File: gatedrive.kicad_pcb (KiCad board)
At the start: 2 copper layers, 50.8 x 54.4 mm, 26 parts, among them IC1 HCPL-316J, IC2 IXDD614PI, p1 POWER SUPPLY CONNECTOR., p2 IGBT CONNECTOR., p3 CONTROLLER CONNECTOR.

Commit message: Prototype
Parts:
- added C4: 0.1uF, Capacitors_ThroughHole:C_Disc_D3_P2.5, F.Cu at (125.7, 122.7)
- added C5: 0.1uF, Capacitors_ThroughHole:C_Disc_D3_P2.5, F.Cu at (140.8, 113.5)
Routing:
- net Net-(D2-Pad2): track 38.5 -> 30.4 mm
- net G: track 94.1 -> 89.0 mm
- net 15V: track 51.4 -> 54.2 mm
- net -5V: track 69.5 -> 72.3 mm
- net Net-(D2-Pad1): track 23.7 -> 21.9 mm
- net Net-(IC1-Pad11): track 54.3 -> 53.2 mm

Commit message: sending to m.n
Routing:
- net MICSUPP: track 23.4 -> 22.8 mm
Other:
- board text removed: "5v"
- board text removed: "T1"
- board text removed: "fault"
- board text removed: "gnd1"
- board text removed: "reset"
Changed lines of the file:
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@@
     (area 106.419714 66.608 183.648286 128.938001)
     (thickness 1.6)
-    (drawings 24)
+    (drawings 19)
     (tracks 135)
     (zones 0)
@@
   )
   (setup
-    (last_trace_width 1.016)
+    (last_trace_width 0.254)
     (user_trace_width 0.254)
     (user_trace_width 0.6)
@@
     (add_net ~RST)
   )
+  (module Socket_Strips:Socket_Strip_Straight_1x05 (layer F.Cu)
+    (at 124.333 79.4385 270)
+    (descr "Through hole socket strip")
+    (tags "socket strip")
+    (fp_text reference p3 (at -3.7846 -4.4196 270) (layer F.SilkS)
+      (effects (font (size 1 1) (thickness 0.15)))
+    )
+    (fp_text value "CONTROLLER CONNECTOR." (at 4.572 -4.064 270) (layer F.Fab)
+      (effects (font (size 1 1) (thickness 0.15)))
+    )
+    (fp_line (start 3.9116 3.2004) (end 3.9116 4.2164) (layer F.SilkS) (width 0.1))
+    (fp_line (start 6.3881 3.2004) (end 6.3881 4.2164) (layer F.SilkS) (width 0.1))
+    (fp_line (start 8.9916 3.2004) (end 8.9916 4.2164) (layer F.SilkS) (width 0.1))
+    (fp_line (start 11.5316 4.2164) (end 11.5316 3.2004) (layer F.SilkS) (width 0.1))
+    (fp_line (start -1.4224 4.2672) (end 11.5316 4.2672) (layer F.SilkS) (width 0.1))
+    (fp_line (start -1.4224 3.2004) (end -1.4224 4.2164) (layer F.SilkS) (width 0.1))
+    (fp_line (start 1.6256 3.2004) (end 1.6256 4.2164) (layer F.SilkS) (width 0.1))
+    (fp_text user ~FAULT (at 0.1143 3.683 270) (layer F.SilkS)
+      (effects (font (size 0.6 0.6) (thickness 0.1)))
+    )
+    (fp_text user T1 (at 10.2743 3.683 270) (layer F.SilkS)
+      (effects (font (size 0.6 0.6) (thickness 0.1)))
+    )
+    (fp_text user ~RST (at 2.6543 3.683 270) (layer F.SilkS)
+      (effects (font (size 0.6 0.6) (thickness 0.1)))
+    )
+    (fp_text user 5V (at 5.1943 3.683 270) (layer F.SilkS)
+      (effects (font (size 0.6 0.6) (thickness 0.1)))
+    )
+    (fp_text user GND1 (at 7.7343 3.683 270) (layer F.SilkS)
+      (effects (font (size 0.6 0.6) (thickness 0.1)))
+    )
+    (fp_line (start -1.8796 3.175) (end -1.8796 -3.429) (layer F.SilkS) (width 0.1))
+    (fp_line (start 12.0142 3.2004) (end -1.8796 3.2004) (layer F.SilkS) (width 0.1))
+    (fp_line (start 12.0142 -3.429) (end 12.0142 3.175) (layer F.SilkS) (width 0.1))
+    (fp_line (start 12.0142 -3.429) (end -1.8796 -3.429) (layer F.SilkS) (width 0.1))
+    (fp_line (start -1.8796 -3.429) (end -1.8796 3.2004) (layer F.CrtYd) (width 0.05))
+    (fp_line (start 12.0142 -3.429) (end 12.0142 3.175) (layer F.CrtYd) (width 0.05))
+    (fp_line (start -1.8796 -3.429) (end 12.0142 -3.429) (layer F.CrtYd) (width 0.05))
+    (fp_line (start -1.8796 3.2004) (end 12.0142 3.2004) (layer F.CrtYd) (width 0.05))
+    (pad 1 thru_hole oval (at 0.0889 0.0254 270) (size 1.7272 2.032) (drill 0.5) (layers *.Cu *.Mask F.SilkS)
+      (net 5 ~FAULT))
+    (pad 2 thru_hole oval (at 2.6289 0.0254 270) (size 1.7272 2.032) (drill 0.5) (layers *.Cu *.Mask F.SilkS)
+      (net 9 ~RST))
+    (pad 3 thru_hole oval (at 5.1689 0.0254 270) (size 1.7272 2.032) (drill 0.5) (layers *.Cu *.Mask F.SilkS)
+      (net 4 MICSUPP))
+    (pad 4 thru_hole oval (at 7.7089 0.0254 270) (size 1.7272 2.032) (drill 0.5) (layers *.Cu *.Mask F.SilkS)
+      (net 7 GND1))
+    (pad 5 thru_hole oval (at 10.2489 0.0254 270) (size 1.7272 2.032) (drill 0.5) (layers *.Cu *.Mask F.SilkS)
+      (net 10 T1))
+    (model Socket_Strips.3dshapes/Socket_Strip_Straight_1x05.wrl
+      (at (xyz 0.2 0 0))
+      (scale (xyz 1 1 1))
+      (rotate (xyz 0 0 180))
+    )
+  )
   (module Capacitors_ThroughHole:C_Disc_D3_P2.5 (layer F.Cu)
     (at 125.73 122.682)
@@
     (descr "Resistor, Axial,  RM 10mm, 1/3W,")
     (tags "Resistor, Axial, RM 10mm, 1/3W,")
-    (fp_text reference R2 (at 0 -2.159) (layer F.SilkS)
+    (fp_text reference R2 (at 0 0) (layer F.SilkS)
       (effects (font (size 1 1) (thickness 0.15)))
     )
@@
       (scale (xyz 0.4 0.4 0.4))
       (rotate (xyz 0 0 0))
-    )
-  )
-  (module Socket_Strips:Socket_Strip_Straight_1x05 (layer F.Cu)
-    (at 124.333 79.4385 270)
-    (descr "Through hole socket strip")
-    (tags "socket strip")
-    (fp_text reference p3 (at -2.3114 0.4445 540) (layer F.SilkS)
-      (effects (font (size 1 1) (thickness 0.15)))
-    )
-    (fp_text value "CONTROLLER CONNECTOR." (at 4.572 -3.556 270) (layer F.Fab)
-      (effects (font (size 1 1) (thickness 0.15)))
-    )
-    (fp_line (start -3.175 -2.54) (end -3.175 3.175) (layer F.CrtYd) (width 0.05))
-    (fp_line (start 13.335 -2.54) (end 13.335 3.2385) (layer F.CrtYd) (width 0.05))
-    (fp_line (start -3.175 -2.54) (end 13.335 -2.54) (layer F.CrtYd) (width 0.05))
-    (fp_line (start -3.175 3.175) (end 13.335 3.2385) (layer F.CrtYd) (width 0.05))
-    (fp_line (start 1.5875 1.651) (end 11.7475 1.651) (layer F.SilkS) (width 0.15))
-    (fp_line (start 11.7475 1.651) (end 11.7475 -0.889) (layer F.SilkS) (width 0.15))
-    (fp_line (start 11.7475 -0.889) (end 1.5875 -0.889) (layer F.SilkS) (width 0.15))
-    (fp_line (start -1.2325 1.931) (end 0.3175 1.931) (layer F.SilkS) (width 0.15))
-    (fp_line (start 1.5875 1.651) (end 1.5875 -0.889) (layer F.SilkS) (width 0.15))
-    (fp_line (start 0.3175 -1.169) (end -1.2325 -1.169) (layer F.SilkS) (width 0.15))
-    (fp_line (start -1.2325 -1.169) (end -1.2325 1.931) (layer F.SilkS) (width 0.15))
-    (pad 1 thru_hole oval (at 0.3175 0.381 270) (size 1.7272 2.032) (drill 0.5) (layers *.Cu *.Mask F.SilkS)
-      (net 5 ~FAULT))
-    (pad 2 thru_hole oval (at 2.8575 0.381 270) (size 1.7272 2.032) (drill 0.5) (layers *.Cu *.Mask F.SilkS)
-      (net 9 ~RST))
-    (pad 3 thru_hole oval (at 5.3975 0.381 270) (size 1.7272 2.032) (drill 0.5) (layers *.Cu *.Mask F.SilkS)
-      (net 4 MICSUPP))
-    (pad 4 thru_hole oval (at 7.9375 0.381 270) (size 1.7272 2.032) (drill 0.5) (layers *.Cu *.Mask F.SilkS)
-      (net 7 GND1))
-    (pad 5 thru_hole oval (at 10.4775 0.381 270) (size 1.7272 2.032) (drill 0.5) (layers *.Cu *.Mask F.SilkS)
-      (net 10 T1))
-    (model Socket_Strips.3dshapes/Socket_Strip_Straight_1x05.wrl
-      (at (xyz 0.2 0 0))
-      (scale (xyz 1 1 1))
-      (rotate (xyz 0 0 180))
     )
   )
@@
     (descr "Capacitor 3mm Disc, Pitch 2.5mm")
     (tags Capacitor)
-    (fp_text reference C1 (at 1.143 -2.286 90) (layer F.SilkS)
+    (fp_text reference C1 (at 1.2046 0.0127 360) (layer F.SilkS)
       (effects (font (size 1 1) (thickness 0.15)))
     )
@@
     (arrow2a (pts (xy 172.466 70.866) (xy 171.879579 71.992504)))
     (arrow2b (pts (xy 172.466 70.866) (xy 173.052421 71.992504)))
-  )
-  (gr_text T1 (at 121.158 89.916) (layer F.SilkS)
-    (effects (font (size 0.7 0.7) (thickness 0.1)))
-  )
-  (gr_text gnd1 (at 121.158 87.376) (layer F.SilkS)
-    (effects (font (size 0.7 0.7) (thickness 0.1)))
-  )
-  (gr_text 5v (at 120.904 84.836) (layer F.SilkS)
-    (effects (font (size 0.7 0.7) (thickness 0.1)))
-  )
-  (gr_text "reset\n" (at 120.904 82.423) (layer F.SilkS)
-    (effects (font (size 0.7 0.7) (thickness 0.1)))
-  )
-  (gr_text "fault\n" (at 120.904 79.756) (layer F.SilkS)
-    (effects (font (size 0.7 0.7) (thickness 0.1)))
   )
   (gr_text G (at 166.497 109.982) (layer F.SilkS)
@@
   (segment (start 141.175 76.835) (end 141.175 76.024) (width 0.635) (layer B.Cu) (net 3) (status 10))
   (segment (start 141.175 76.024) (end 139.446 74.295) (width 0.635) (layer B.Cu) (net 3) (status 20))
-  (segment (start 122.34164 73.533) (end 123.117999 74.309359) (width 1.27) (layer B.Cu) (net 4) (status 10))
-  (segment (start 123.117999 74.309359) (end 123.117999 76.780001) (width 1.27) (layer B.Cu) (net 4))
+  (segment (start 122.722067 84.836) (end 123.952 84.836) (width 1.27) (layer B.Cu) (net 4))
   (segment (start 121.881127 83.99506) (end 122.722067 84.836) (width 1.27) (layer B.Cu) (net 4))
-  (segment (start 123.117999 76.780001) (end 121.881127 78.016873) (width 1.27) (layer B.Cu) (net 4))
   (segment (start 121.881127 78.016873) (end 121.881127 83.99506) (width 1.27) (layer B.Cu) (net 4))
-  (segment (start 122.722067 84.836) (end 123.952 84.836) (width 1.27) (layer B.Cu) (net 4) (status 20))
+  (segment (start 122.350617 77.547383) (end 121.881127 78.016873) (width 1.27) (layer B.Cu) (net 4))
+  (segment (start 122.350617 73.541977) (end 122.350617 77.547383) (width 1.27) (layer B.Cu) (net 4))
+  (segment (start 122.34164 73.533) (end 122.350617 73.541977) (width 1.27) (layer B.Cu) (net 4))
   (segment (start 129.2225 81.875) (end 130.5325 83.185) (width 0.6) (layer B.Cu) (net 4) (status 10))
   (segment (start 130.5325 83.185) (end 131.875 83.185) (width 0.6) (layer B.Cu) (net 4) (status 20))

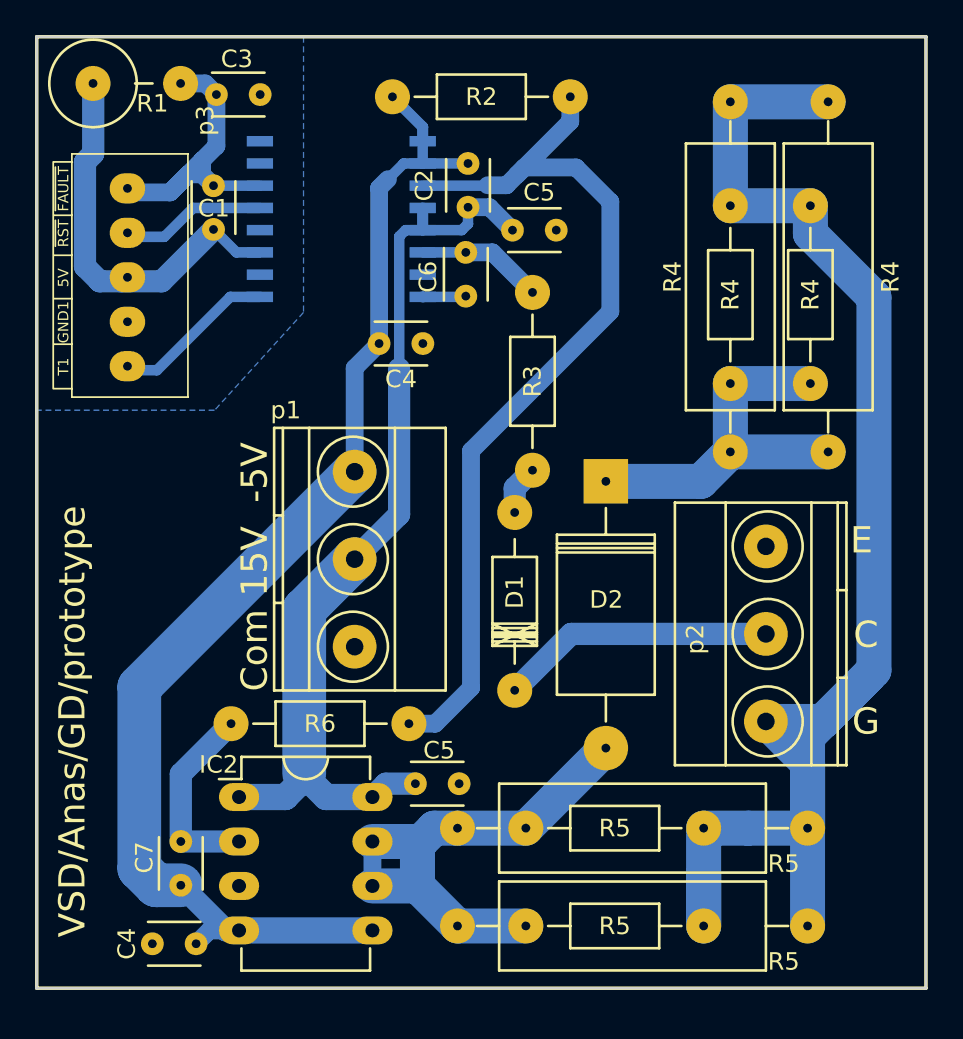
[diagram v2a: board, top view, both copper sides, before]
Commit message: updsting hcpl-316j ic footprint and layout
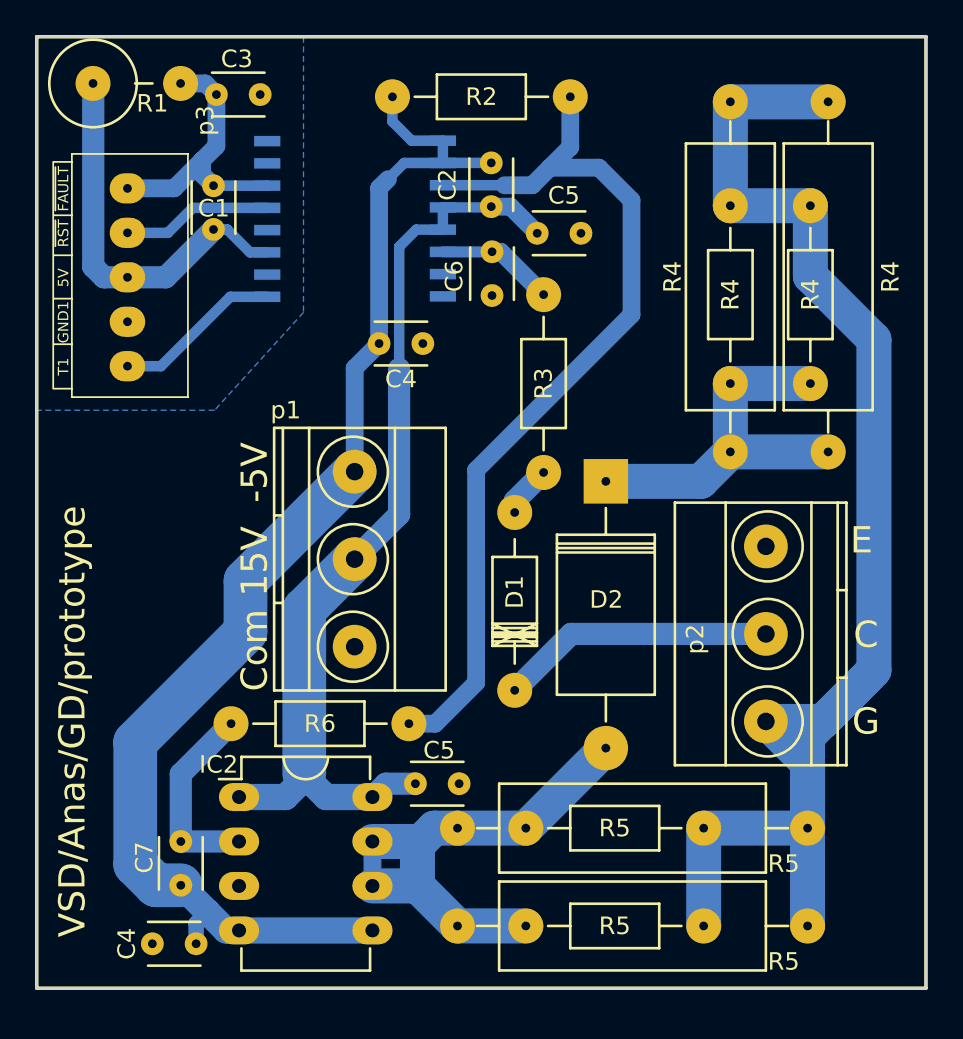
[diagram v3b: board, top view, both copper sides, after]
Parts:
- moved C6 1.50 mm to (145.1, 83.1)
- moved C5 1.42 mm to (147.7, 82.1)
- moved C2 1.33 mm to (145.1, 80.6)
- moved IC1 1.15 mm to (137.7, 81.3)
- moved R3 0.65 mm to (148.1, 90.7)
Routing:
- net G: track 89.0 -> 85.9 mm
- net COM: track 2.49 -> 0.07 mm
- net -5V: track 72.3 -> 74.6 mm
- net ~FAULT: track 18.4 -> 16.1 mm
- net Net-(IC1-Pad11): track 53.2 -> 52.6 mm

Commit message: cleaning the repo
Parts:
- removed C4 (x2): 0.1uF, Capacitors_ThroughHole:C_Disc_D3_P2.5
- removed the C5 at (140.8, 113.5)
- removed the C5 at (147.7, 82.1)
- removed the R4 at (163.3, 85.6)
- removed the R4 at (158.8, 84.6)
- removed the R4 at (164.3, 84.6)
- removed the R4 at (158.8, 85.6)
- removed the R5 at (152.1, 116.1)
- removed the R5 at (153.2, 121.7)
- removed the R5 at (153.2, 116.1)
- removed the R5 at (152.1, 121.7)
- removed p1: POWER SUPPLY CONNECTOR., Terminal_Blocks:TerminalBlock_Pheonix_MKDS1.5-3pol
- removed p2: IGBT CONNECTOR., Terminal_Blocks:TerminalBlock_Pheonix_MKDS1.5-3pol
- removed p3: CONTROLLER CONNECTOR., Socket_Strips:Socket_Strip_Straight_1x05
- added C10: 100pF, gatedrive:C_Disc, F.Cu at (68.9, 75.0)
- added C11: 330pF, gatedrive:C_Disc, F.Cu at (61.3, 66.1)
- added C11: 330pF, gatedrive:C_Disc, F.Cu at (116.5, 44.5)
- added C12: 10nF, gatedrive:C_Disc, F.Cu at (75.2, 80.1)
- added C13: 0.1uF, gatedrive:C_Disc, F.Cu at (75.2, 77.6)
- added C14: 0.1uF, gatedrive:C_Disc, F.Cu at (66.3, 71.2)
- added C15: 0.1uF, gatedrive:C_Disc, F.Cu at (222.5, 62.3)
- added C16: 0.1uF, gatedrive:C_Disc, F.Cu at (98.7, 75.0)
- added C17: 100pF, gatedrive:C_Disc, F.Cu at (92.4, 75.0)
- added C19: 10nF, gatedrive:C_Disc, F.Cu at (98.7, 77.6)
- added C20: 0.1uF, gatedrive:C_Disc, F.Cu at (98.7, 80.1)
- added C21: 0.1uF, gatedrive:C_Disc, F.Cu at (89.8, 71.2)
- added C22: 0.1uF, gatedrive:C_Disc, F.Cu at (114.0, 62.3)
- added C23: 0.1uF, gatedrive:C_Disc, F.Cu at (120.9, 75.0)
- added C24: 100pF, gatedrive:C_Disc, F.Cu at (118.4, 75.0)
- added C26: 10nF, gatedrive:C_Disc, F.Cu at (126.0, 78.8)
- added C27: 0.1uF, gatedrive:C_Disc, F.Cu at (123.5, 78.8)
- added C28: 0.1uF, gatedrive:C_Disc, F.Cu at (114.0, 71.2)
- added C29: 0.1uF, gatedrive:C_Disc, F.Cu at (176.2, 62.3)
- added C30: 0.1uF, gatedrive:C_Disc, F.Cu at (51.7, 75.0)
- added C31: 100pF, gatedrive:C_Disc, F.Cu at (45.4, 75.0)
- added C32: 330pF, gatedrive:C_Disc, F.Cu at (129.2, 66.1)
- added C33: 10nF, gatedrive:C_Disc, F.Cu at (51.7, 80.1)
- added C34: 0.1uF, gatedrive:C_Disc, F.Cu at (51.7, 77.6)
- added C35: 0.1uF, gatedrive:C_Disc, F.Cu at (42.2, 71.2)
- added C36: 0.1uF, gatedrive:C_Disc, F.Cu at (152.7, 62.3)
- added C37: 0.1uF, gatedrive:C_Disc, F.Cu at (144.4, 75.0)
- added C38: 100pF, gatedrive:C_Disc, F.Cu at (139.4, 78.8)
- added C40: 10nF, gatedrive:C_Disc, F.Cu at (149.5, 78.8)
- added C41: 0.1uF, gatedrive:C_Disc, F.Cu at (147.0, 78.8)
- added C42: 0.1uF, gatedrive:C_Disc, F.Cu at (141.9, 75.0)
- added C43: 0.1uF, gatedrive:C_Disc, F.Cu at (105.3, 62.3)
- added C44: 0.1uF, gatedrive:C_Disc, F.Cu at (163.5, 79.5)
- added C45: 100pF, gatedrive:C_Disc, F.Cu at (160.3, 74.4)
- added C47: 10nF, gatedrive:C_Disc, F.Cu at (173.6, 79.5)
- added C48: 0.1uF, gatedrive:C_Disc, F.Cu at (169.2, 76.3)
- added C49: 0.1uF, gatedrive:C_Disc, F.Cu at (166.7, 76.3)
- added C5: 10nF, gatedrive:C_Disc, F.Cu at (209.8, 89.6)
- added C50: 0.1uF, gatedrive:C_Disc, F.Cu at (81.8, 62.3)
- added C51: 0.1uF, gatedrive:C_Disc, F.Cu at (193.3, 75.7)
- added C52: 100pF, gatedrive:C_Disc, F.Cu at (190.8, 75.7)
- added C53: 330pF, gatedrive:C_Disc, F.Cu at (226.4, 66.1)
- added C54: 10nF, gatedrive:C_Disc, F.Cu at (188.9, 89.0)
- added C55: 0.1uF, gatedrive:C_Disc, F.Cu at (193.3, 79.5)
- added C56: 0.1uF, gatedrive:C_Disc, F.Cu at (190.8, 79.5)
- added C8: 0.1uF, gatedrive:C_Disc, F.Cu at (58.3, 62.3)
- added C9: 0.1uF, gatedrive:C_Disc, F.Cu at (75.2, 75.0)
- added D10: ~, Diodes_ThroughHole:Diode_DO-201AD_Horizontal_RM15, F.Cu at (51.7, 109.9)
- added D11: RGPO2-20, Diodes_ThroughHole:Diode_DO-201AD_Horizontal_RM15, F.Cu at (136.8, 101.7)
- added D12: ~, Diodes_ThroughHole:Diode_DO-201AD_Horizontal_RM15, F.Cu at (145.7, 112.5)
- added D13: RGPO2-20, Diodes_ThroughHole:Diode_DO-201AD_Horizontal_RM15, F.Cu at (161.0, 106.8)
- added D14: ~, Diodes_ThroughHole:Diode_DO-201AD_Horizontal_RM15, F.Cu at (168.6, 116.9)
- added D15: RGPO2-20, Diodes_ThroughHole:Diode_DO-201AD_Horizontal_RM15, F.Cu at (183.8, 99.8)
- added D16: ~, Diodes_ThroughHole:Diode_DO-201AD_Horizontal_RM15, F.Cu at (195.9, 112.5)
- added D17: LED, LEDs:LED-3MM, F.Cu at (67.0, 43.3)
- added D18: LED, LEDs:LED-3MM, F.Cu at (60.8, 43.3)
- added D19: LED, LEDs:LED-3MM, F.Cu at (54.9, 43.3)
- added D3: RGPO2-20, Diodes_ThroughHole:Diode_DO-201AD_Horizontal_RM15, F.Cu at (67.0, 108.0)
- added D4: ~, Diodes_ThroughHole:Diode_DO-201AD_Horizontal_RM15, F.Cu at (72.7, 112.5)
- added D5: RGPO2-20, Diodes_ThroughHole:Diode_DO-201AD_Horizontal_RM15, F.Cu at (89.8, 108.0)
- added D6: ~, Diodes_ThroughHole:Diode_DO-201AD_Horizontal_RM15, F.Cu at (102.5, 131.5)
- added D7: RGPO2-20, Diodes_ThroughHole:Diode_DO-201AD_Horizontal_RM15, F.Cu at (113.4, 108.5)
- added D8: ~, Diodes_ThroughHole:Diode_DO-201AD_Horizontal_RM15, F.Cu at (126.0, 113.1)
- added D9: RGPO2-20, Diodes_ThroughHole:Diode_DO-201AD_Horizontal_RM15, F.Cu at (42.8, 108.0)
- added IC10: IXDD614PI, gatedrive:DIP-8_W7.62mm_LongPads, F.Cu at (47.9, 84.5)
- added IC11: HCPL-316J, Housings_SOIC:SOIC-16_7.5x10.3mm_Pitch1.27mm, B.Cu at (144.7, 67.6)
- added IC12: IXDD614PI, gatedrive:DIP-8_W7.62mm_LongPads, F.Cu at (142.0, 84.9)
- added IC13: HCPL-316J, Housings_SOIC:SOIC-16_7.5x10.3mm_Pitch1.27mm, B.Cu at (168.3, 67.6)
- added IC14: IXDD614PI, gatedrive:DIP-8_W7.62mm_LongPads, F.Cu at (176.2, 94.1)
- added IC15: HCPL-316J, Housings_SOIC:SOIC-16_7.5x10.3mm_Pitch1.27mm, B.Cu at (191.9, 67.6)
- added IC16: IXDD614PI, gatedrive:DIP-8_W7.62mm_LongPads, F.Cu at (192.1, 85.8)
- added IC3: HCPL-316J, Housings_SOIC:SOIC-16_7.5x10.3mm_Pitch1.27mm, B.Cu at (73.8, 67.6)
- added IC4: IXDD614PI, gatedrive:DIP-8_W7.62mm_LongPads, F.Cu at (71.4, 84.5)
- added IC5: HCPL-316J, Housings_SOIC:SOIC-16_7.5x10.3mm_Pitch1.27mm, B.Cu at (97.4, 67.6)
- added IC6: IXDD614PI, gatedrive:DIP-8_W7.62mm_LongPads, F.Cu at (94.9, 84.5)
- added IC7: HCPL-316J, Housings_SOIC:SOIC-16_7.5x10.3mm_Pitch1.27mm, B.Cu at (121.1, 67.6)
- added IC8: IXDD614PI, gatedrive:DIP-8_W7.62mm_LongPads, F.Cu at (118.5, 83.9)
- added IC9: HCPL-316J, Housings_SOIC:SOIC-16_7.5x10.3mm_Pitch1.27mm, B.Cu at (50.2, 67.6)
- added P1: Mic General Connector, Socket_Strips:Socket_Strip_Angled_1x12, F.Cu at (147.6, 44.5)
- added P10: CONN_01X03, Pin_Headers:Pin_Header_Angled_1x03, F.Cu at (77.8, 134.7)
- added P11: CONN_01X03, Pin_Headers:Pin_Header_Angled_1x03, F.Cu at (67.3, 134.7)
- added P12: CONN_01X03, Pin_Headers:Pin_Header_Angled_1x03, F.Cu at (88.4, 134.7)
- added P13: CONN_01X03, Pin_Headers:Pin_Header_Angled_1x03, F.Cu at (98.9, 134.7)
- added P14: CONN_01X03, Pin_Headers:Pin_Header_Angled_1x03, F.Cu at (165.4, 134.7)
- added P15: CONN_01X03, Pin_Headers:Pin_Header_Angled_1x03, F.Cu at (176.8, 134.7)
- added P16: CONN_01X03, Pin_Headers:Pin_Header_Angled_1x03, F.Cu at (188.3, 134.7)
- added P17: CONN_01X03, Pin_Headers:Pin_Header_Angled_1x03, F.Cu at (204.0, 134.7)
- added P2: CONN_01X03, Pin_Headers:Pin_Header_Angled_1x03, F.Cu at (214.6, 134.7)
- added P3: CONN_01X03, Pin_Headers:Pin_Header_Angled_1x03, F.Cu at (225.1, 134.7)
- added P4: CONN_01X03, Pin_Headers:Pin_Header_Angled_1x03, F.Cu at (129.2, 134.7)
- added P5: CONN_01X03, Pin_Headers:Pin_Header_Angled_1x03, F.Cu at (119.0, 134.7)
- added P6: CONN_01X03, Pin_Headers:Pin_Header_Angled_1x03, F.Cu at (140.9, 134.7)
- added P7: CONN_01X03, Pin_Headers:Pin_Header_Angled_1x03, F.Cu at (150.8, 134.7)
- added P8: CONN_01X03, Pin_Headers:Pin_Header_Angled_1x03, F.Cu at (44.6, 126.6)
- added P9: CONN_01X03, Pin_Headers:Pin_Header_Angled_1x03, F.Cu at (56.8, 134.7)
- added R10: 100, Resistors_ThroughHole:Resistor_Horizontal_RM10mm, F.Cu at (82.2, 82.0)
- added R11: 60, gatedrive:Resistor_multi, F.Cu at (78.4, 127.7)
- added R12: 30ohm ,0.5W, gatedrive:Resistor_multi, F.Cu at (83.5, 95.3)
- added R13: 10K, Resistors_ThroughHole:Resistor_Horizontal_RM10mm, F.Cu at (53.0, 56.6)
- added R14: 25K, Resistors_ThroughHole:Resistor_Horizontal_RM10mm, F.Cu at (108.2, 82.0)
- added R15: 100, Resistors_ThroughHole:Resistor_Horizontal_RM10mm, F.Cu at (89.8, 78.8)
- added R16: 100, Resistors_ThroughHole:Resistor_Horizontal_RM10mm, F.Cu at (105.7, 82.0)
- added R17: 60, gatedrive:Resistor_multi, F.Cu at (98.1, 99.8)
- added R18: 30ohm ,0.5W, gatedrive:Resistor_multi, F.Cu at (107.0, 92.8)
- added R19: 10K, Resistors_ThroughHole:Resistor_Horizontal_RM10mm, F.Cu at (100.0, 56.6)
- added R20: 25K, Resistors_ThroughHole:Resistor_Horizontal_RM10mm, F.Cu at (131.7, 82.0)
- added R21: 100, Resistors_ThroughHole:Resistor_Horizontal_RM10mm, F.Cu at (113.3, 78.8)
- added R22: 100, Resistors_ThroughHole:Resistor_Horizontal_RM10mm, F.Cu at (129.2, 82.0)
- added R23: 60, gatedrive:Resistor_multi, F.Cu at (130.5, 101.7)
- added R24: 30ohm ,0.5W, gatedrive:Resistor_multi, F.Cu at (120.1, 108.2)
- added R25: 10K, Resistors_ThroughHole:Resistor_Horizontal_RM10mm, F.Cu at (165.4, 56.6)
- added R26: 25K, Resistors_ThroughHole:Resistor_Horizontal_RM10mm, F.Cu at (61.3, 82.0)
- added R27: 100, Resistors_ThroughHole:Resistor_Horizontal_RM10mm, F.Cu at (42.2, 78.7)
- added R28: 100, Resistors_ThroughHole:Resistor_Horizontal_RM10mm, F.Cu at (58.7, 82.0)
- added R29: 60, gatedrive:Resistor_multi, F.Cu at (56.8, 109.9)
- added R30: 30ohm ,0.5W, gatedrive:Resistor_multi, F.Cu at (61.3, 87.1)
- added R31: 10K, Resistors_ThroughHole:Resistor_Horizontal_RM10mm, F.Cu at (212.1, 56.6)
- added R32: 25K, Resistors_ThroughHole:Resistor_Horizontal_RM10mm, F.Cu at (155.2, 80.7)
- added R33: 100, Resistors_ThroughHole:Resistor_Horizontal_RM10mm, F.Cu at (136.2, 71.8)
- added R34: 100, Resistors_ThroughHole:Resistor_Horizontal_RM10mm, F.Cu at (152.7, 80.7)
- added R35: 60, gatedrive:Resistor_multi, F.Cu at (136.8, 109.3)
- added R36: 30ohm ,0.5W, gatedrive:Resistor_multi, F.Cu at (153.3, 97.2)
- added R37: 10K, Resistors_ThroughHole:Resistor_Horizontal_RM10mm, F.Cu at (74.6, 56.6)
- added R38: 25K, Resistors_ThroughHole:Resistor_Horizontal_RM10mm, F.Cu at (178.7, 80.7)
- added R39: 100, Resistors_ThroughHole:Resistor_Horizontal_RM10mm, F.Cu at (160.3, 78.2)
- added R4: 100, Resistors_ThroughHole:Resistor_Horizontal_RM10mm, F.Cu at (223.2, 80.7)
- added R40: 100, Resistors_ThroughHole:Resistor_Horizontal_RM10mm, F.Cu at (176.2, 80.7)
- added R41: 60, gatedrive:Resistor_multi, F.Cu at (161.6, 110.6)
- added R42: 30ohm ,0.5W, gatedrive:Resistor_multi, F.Cu at (178.1, 99.8)
- added R43: 10K, Resistors_ThroughHole:Resistor_Horizontal_RM10mm, F.Cu at (188.9, 56.6)
- added R44: 25K, Resistors_ThroughHole:Resistor_Horizontal_RM10mm, F.Cu at (202.2, 80.7)
- added R45: 100, Resistors_ThroughHole:Resistor_Horizontal_RM10mm, F.Cu at (183.8, 70.6)
- added R46: 100, Resistors_ThroughHole:Resistor_Horizontal_RM10mm, F.Cu at (199.7, 80.7)
- added R47: 60, gatedrive:Resistor_multi, F.Cu at (190.2, 103.0)
- added R48: 30ohm ,0.5W, gatedrive:Resistor_multi, F.Cu at (201.0, 97.9)
- added R49: R, Resistors_SMD:R_1206, B.Cu at (65.5, 47.1)
- added R5: 60, gatedrive:Resistor_multi, F.Cu at (213.7, 104.9)
- added R50: R, Resistors_SMD:R_1206, B.Cu at (59.3, 47.1)
- added R51: R, Resistors_SMD:R_1206, B.Cu at (51.7, 44.7)
- added R7: 10K, Resistors_ThroughHole:Resistor_Horizontal_RM10mm, F.Cu at (133.6, 56.0)
- added R8: 25K, Resistors_ThroughHole:Resistor_Horizontal_RM10mm, F.Cu at (84.7, 82.0)
- added R9: 100, Resistors_ThroughHole:Resistor_Horizontal_RM10mm, F.Cu at (66.3, 78.8)
- added REF**: MountingHole_3-5mm, Mounting_Holes:MountingHole_3-5mm, F.Cu at (43.5, 42.6)
- added REF**: MountingHole_3-5mm, Mounting_Holes:MountingHole_3-5mm, F.Cu at (44.1, 135.3)
- added REF**: MountingHole_3-5mm, Mounting_Holes:MountingHole_3-5mm, F.Cu at (235.2, 135.3)
- added REF**: MountingHole_3-5mm, Mounting_Holes:MountingHole_3-5mm, F.Cu at (235.2, 42.6)
- C1, C2: footprint Capacitors_ThroughHole:C_Disc_D3_P2.5 -> gatedrive:C_Disc
- C3: value 330pF -> 100pF; footprint Capacitors_ThroughHole:C_Disc_D3_P2.5 -> gatedrive:C_Disc
- C6: value 100pF -> 0.1uF; footprint Capacitors_ThroughHole:C_Disc_D3_P2.5 -> gatedrive:C_Disc
- C7: value 10nF -> 0.1uF; footprint Capacitors_ThroughHole:C_Disc_D3_P2.5 -> gatedrive:C_Disc
- D1: footprint Diodes_ThroughHole:Diode_DO-41_SOD81_Horizontal_RM10 -> Diodes_ThroughHole:Diode_DO-201AD_Horizontal_RM15
- D2: value 1N5821 -> ~
- R1: footprint Resistors_ThroughHole:Resistor_Vertical_RM5mm -> Resistors_ThroughHole:Resistor_Horizontal_RM10mm
- R6: value 100 -> 30ohm ,0.5W; footprint Resistors_ThroughHole:Resistor_Horizontal_RM10mm -> gatedrive:Resistor_multi
- moved C7 94.8 mm to (213.0, 76.3)
- moved IC2 87.7 mm to (213.7, 85.8)
- moved R6 84.9 mm to (219.4, 98.5), turned to 270 degrees
- moved R2 81.4 mm to (225.7, 80.7), turned to 90 degrees
- moved C3 81.1 mm to (210.2, 80.1), turned to 90 degrees
- moved IC1 79.1 mm to (215.6, 67.6), turned to 270 degrees
- moved D2 75.5 mm to (225.1, 113.8), turned to 90 degrees
- moved C1 73.1 mm to (199.7, 62.3), turned to 270 degrees
- moved C2 70.6 mm to (215.6, 76.3), turned to 0 degrees
- moved C6 70.5 mm to (215.6, 80.1), turned to 0 degrees
- moved R3 62.3 mm to (207.3, 71.2)
- moved D1 61.5 mm to (207.3, 99.2)
- moved R1 25.9 mm to (144.4, 56.6)
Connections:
- C2 pad 1: 15V -> 15v1
- C2 pad 2: -5V -> -5V1
- C3 pad 1: ~FAULT -> Net-(C3-Pad1)
- C3 pad 2: GND1 -> COM1
- C6 pad 1: Net-(C6-Pad1) -> COM1
- C6 pad 2: COM -> -5V1
- C7 pad 1: Net-(C7-Pad1) -> 15v1
- C7 pad 2: -5V -> COM1
- D1 pad 1: C -> C1
- IC1 pad 10: -5V -> -5V1
- IC1 pad 12: 15V -> 15v1
- IC1 pad 13: 15V -> 15v1
- IC1 pad 14: Net-(C6-Pad1) -> Net-(C3-Pad1)
- IC1 pad 15: (no net) -> Net-(IC1-Pad15)
- IC1 pad 16: COM -> COM1
- IC1 pad 7: (no net) -> Net-(IC1-Pad7)
- IC1 pad 9: -5V -> -5V1
- IC2 pad 1: 15V -> 15v1
- IC2 pad 2: Net-(C7-Pad1) -> Net-(C5-Pad1)
- IC2 pad 3: (no net) -> 15v1
- IC2 pad 4: -5V -> -5V1
- IC2 pad 5: -5V -> -5V1
- IC2 pad 8: 15V -> 15v1
- R2 pad 1: -5V -> -5V1
- R3 pad 1: Net-(C6-Pad1) -> Net-(C3-Pad1)
- R6 pad 1: Net-(C7-Pad1) -> Net-(D2-Pad2)
- R6 pad 2: Net-(IC1-Pad11) -> G1
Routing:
- net ~FAULT: track 16.1 -> 349.6 mm
- net ~RST: track 8.57 -> 246.9 mm, vias 0 -> 8
- net -5V1: track 0.00 -> 109.5 mm
- net /T8: track 0.00 -> 90.8 mm
- net G: track 85.9 -> 0.00 mm
- net -5V: track 74.6 -> 0.00 mm
- net -5v8: track 0.00 -> 73.8 mm, vias 0 -> 1
- net /T7: track 0.00 -> 71.7 mm
- net T1: track 9.63 -> 79.8 mm
- net -5V2: track 0.00 -> 67.1 mm
- net /T2: track 0.00 -> 59.6 mm
- net 15V: track 54.3 -> 0.00 mm
- net /T6: track 0.00 -> 50.0 mm
- net -5V7: track 0.00 -> 47.1 mm
- net C1: track 0.00 -> 46.1 mm
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- added copper zone on F.Cu, net -5V2
- added copper zone on B.Cu, net -5V3
- added copper zone on B.Cu, net -5V7
- added copper zone on B.Cu, net -5v8
- added copper zone on B.Cu, net 15V2
- added copper zone on B.Cu, net 15V3
- added copper zone on B.Cu, net 15V4
- added copper zone on B.Cu, net 15V5
- added copper zone on B.Cu, net 15V6
- added copper zone on B.Cu, net 15V7
- added copper zone on B.Cu, net 15V8
- added copper zone on B.Cu, net 15v1
- added copper zone on F.Cu, net COM1
- added copper zone on F.Cu, net COM2
- added copper zone on F.Cu, net COM3
- added copper zone on F.Cu, net COM5
- added copper zone on F.Cu, net COM6
- added copper zone on F.Cu, net COM7
- added copper zone on F.Cu, net COM8
- added copper zone on F.Cu, net MICSUPP
- removed copper zone on B.Cu, net COM
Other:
- board size 50.8 x 54.4 mm -> 200.7 x 101.6 mm
- net class Default: via_dia 0.6 -> 2
- net class Gate signal added: clearance 0.2, trace_width 2, via_dia 2, via_drill 0.4
- board text removed: "-5V"
- board text removed: "14A IGBT GATE DRIVER BASED ON IXDD614PI AND HCPL-316J"
- board text removed: "15V"
- board text removed: "C"
- board text removed: "Com"
- board text removed: "E"
- board text removed: "G"
- board text removed: "VSD/Anas/GD/prototype"
- board text removed: "note that gate resistors are easily scalabe to different IGBT sizes."
